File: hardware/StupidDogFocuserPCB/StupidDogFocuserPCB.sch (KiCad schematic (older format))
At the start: 17 parts, among them M1 Stepper_Motor_bipolar, SW1 Rotary_Encoder_Switch, U1 DHT11, U2 SN74HC14N

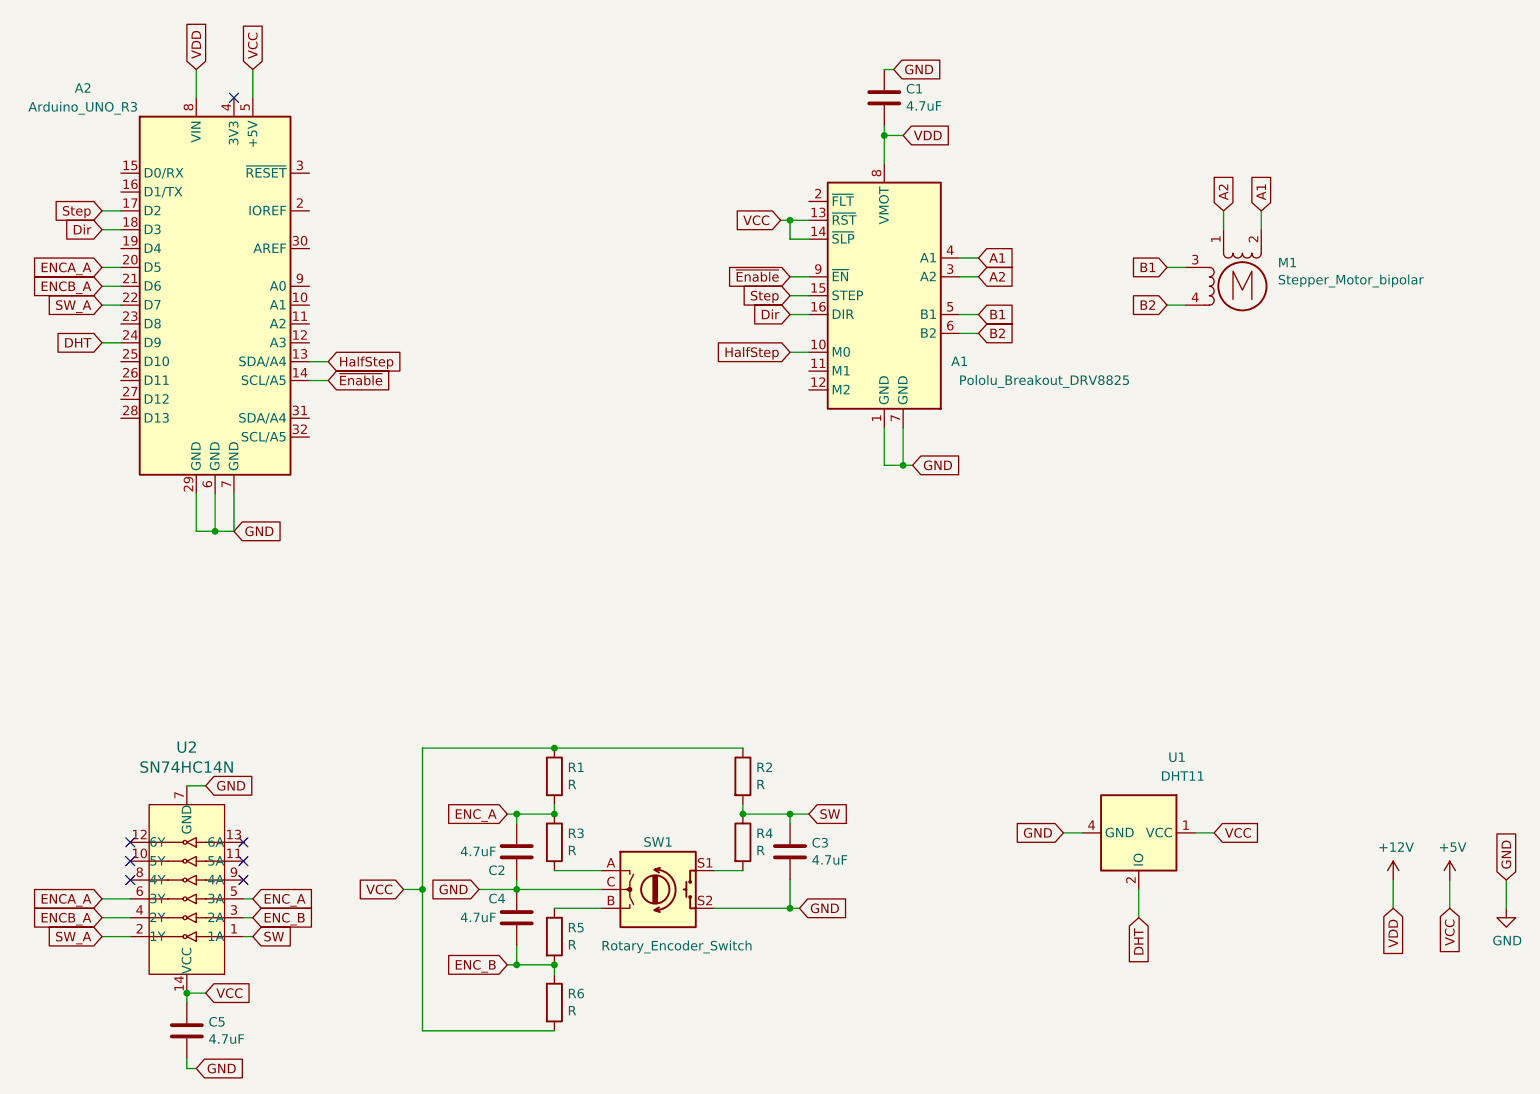
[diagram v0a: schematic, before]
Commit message: Remapped kicad pins. Still need to map firmware.
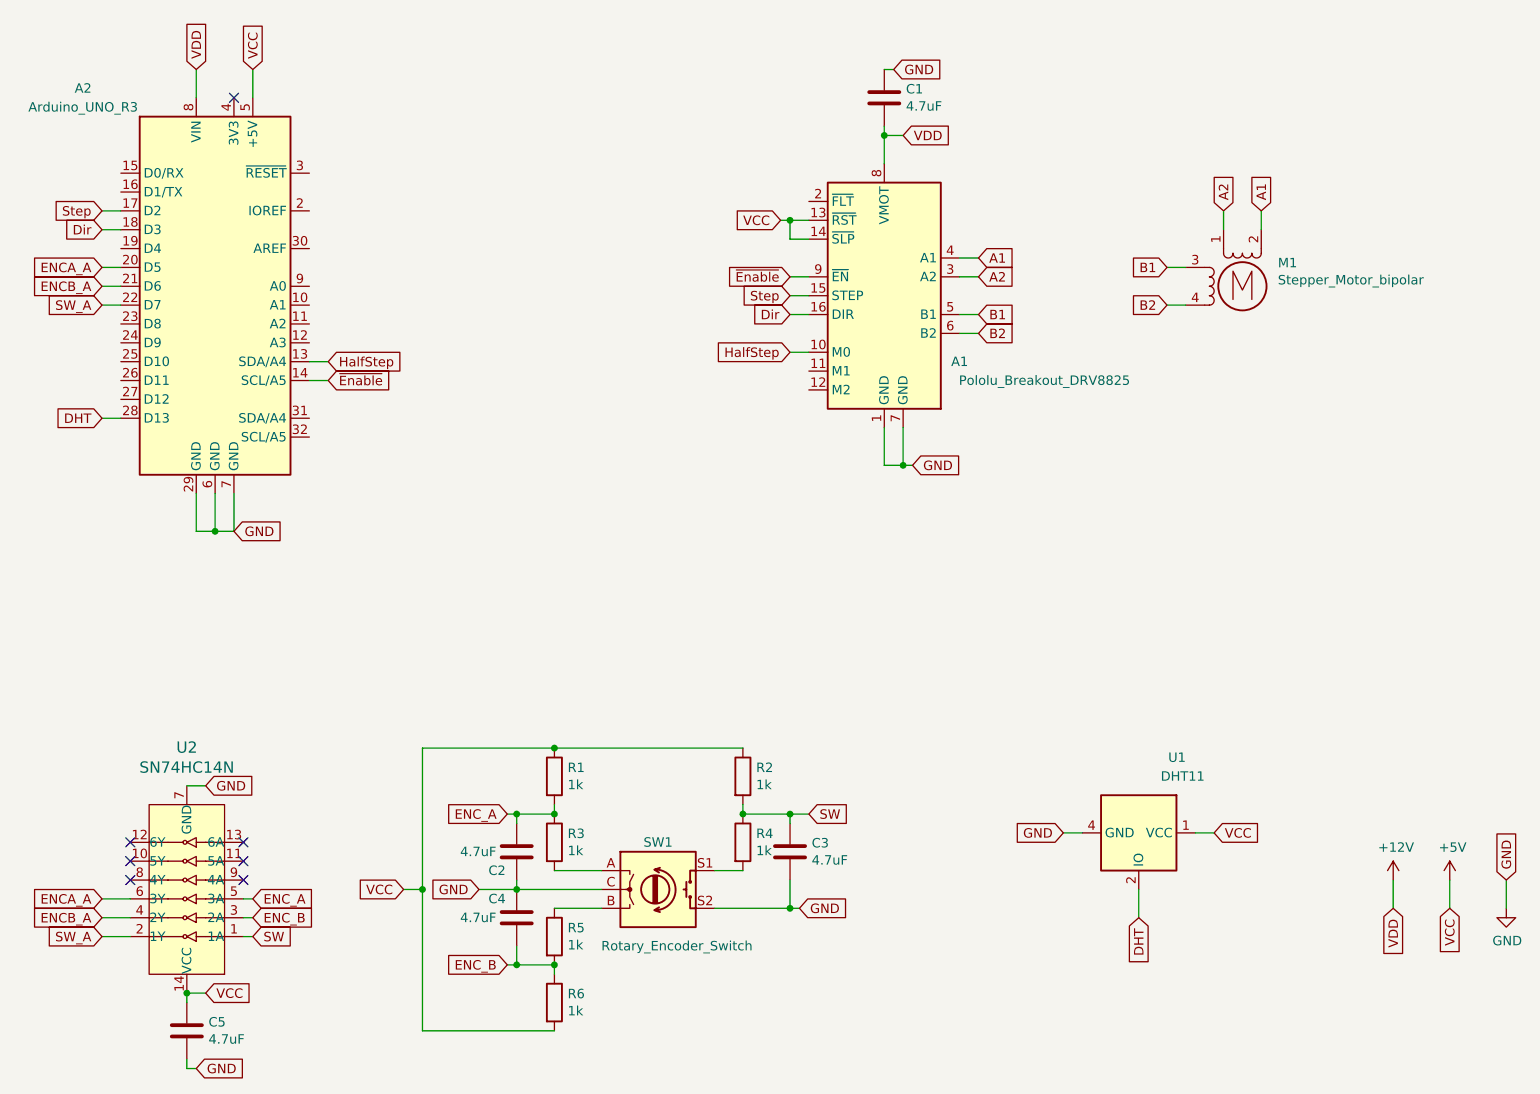
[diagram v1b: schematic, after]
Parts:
- R1, R2, R3, R4, R5, R6: value R -> 1k
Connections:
- net DHT: now also A2.28 (D13); no longer A2.24 (D9)
